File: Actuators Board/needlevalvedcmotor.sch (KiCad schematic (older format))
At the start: 46 parts, among them J10 Conn_01x02_Male, J9 Conn_01x02_Male, Q1 MMDT2222A

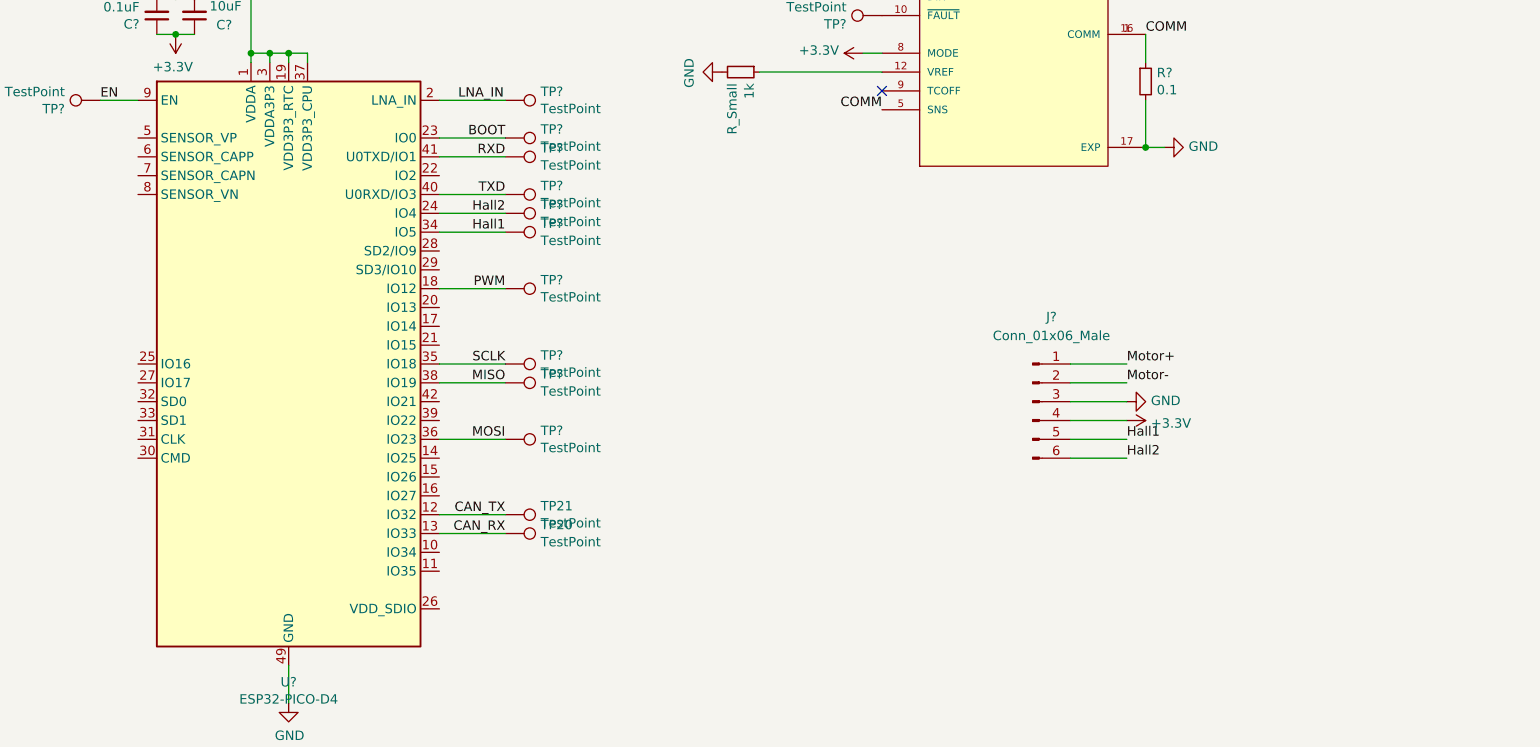
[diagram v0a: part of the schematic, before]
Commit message: Added power connectors for needlevalve
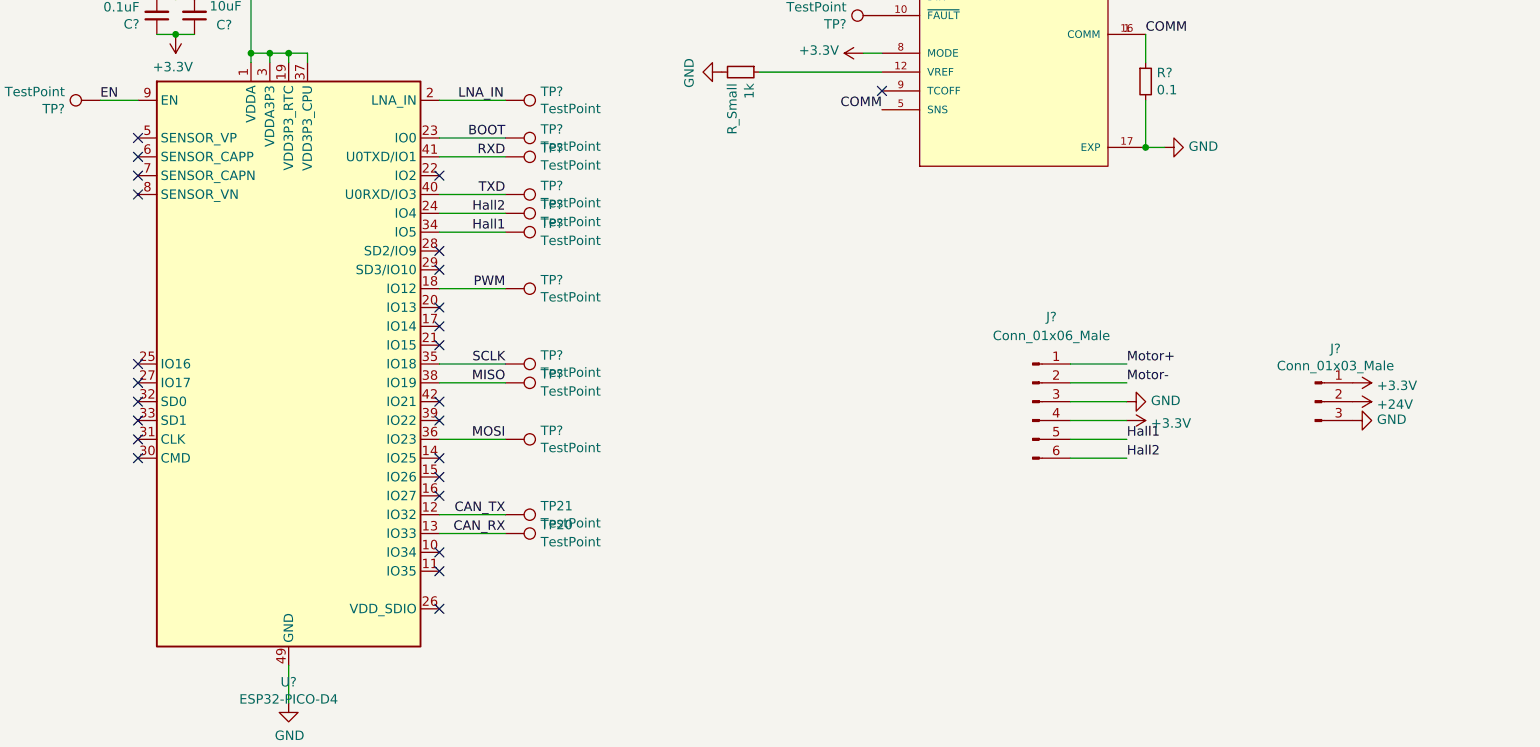
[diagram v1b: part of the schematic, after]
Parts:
- added J?: Conn_01x03_Male, symbol Connector:Conn_01x03_Male
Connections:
- net +24V: now also J?.2 (Pin_2)
- net +3V3: now also J?.1 (Pin_1)
- net GND: now also J?.3 (Pin_3)
- no-connect marks 1 -> 25
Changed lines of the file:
@@
 Wire Wire Line
 	5000 2150 5350 2150
+NoConn ~ 5000 3250
+NoConn ~ 5000 3350
+NoConn ~ 5000 3450
+NoConn ~ 5000 3750
+NoConn ~ 5000 3850
+NoConn ~ 5000 4050
+NoConn ~ 5000 4150
+NoConn ~ 5000 4250
+NoConn ~ 5000 4550
+NoConn ~ 5000 4650
+NoConn ~ 5000 4850
+NoConn ~ 5000 2550
+NoConn ~ 5000 2950
+NoConn ~ 5000 3050
+NoConn ~ 3400 3550
+NoConn ~ 3400 3650
+NoConn ~ 3400 3750
+NoConn ~ 3400 3850
+NoConn ~ 3400 3950
+NoConn ~ 3400 4050
+NoConn ~ 3400 2650
+NoConn ~ 3400 2550
+NoConn ~ 3400 2450
+NoConn ~ 3400 2350
+$Comp
+L Connector:Conn_01x03_Male J?
+U 1 1 61B4C445
+P 9650 3750
+F 0 "J?" H 9758 4031 50  0000 C CNN
+F 1 "Conn_01x03_Male" H 9758 3940 50  0000 C CNN
+F 2 "" H 9650 3750 50  0001 C CNN
+F 3 "~" H 9650 3750 50  0001 C CNN
+	1    9650 3750
+	1    0    0    -1
+$EndComp
+$Comp
+L power:+3.3V #PWR?
+U 1 1 61B4D2E9
+P 9850 3650
+F 0 "#PWR?" H 9850 3500 50  0001 C CNN
+F 1 "+3.3V" V 9865 3778 50  0000 L CNN
+F 2 "" H 9850 3650 50  0001 C CNN
+F 3 "" H 9850 3650 50  0001 C CNN
+	1    9850 3650
+	0    1    1    0
+$EndComp
+$Comp
+L power:GND #PWR?
+U 1 1 61B4E2F5
+P 9850 3850
+F 0 "#PWR?" H 9850 3600 50  0001 C CNN
+F 1 "GND" V 9855 3722 50  0000 R CNN
+F 2 "" H 9850 3850 50  0001 C CNN
+F 3 "" H 9850 3850 50  0001 C CNN
+	1    9850 3850
+	0    -1   -1   0
+$EndComp
+$Comp
+L power:+24V #PWR?
+U 1 1 61B4EDFF
+P 9850 3750
+F 0 "#PWR?" H 9850 3600 50  0001 C CNN
+F 1 "+24V" V 9865 3878 50  0000 L CNN
+F 2 "" H 9850 3750 50  0001 C CNN
+F 3 "" H 9850 3750 50  0001 C CNN
+	1    9850 3750
+	0    1    1    0
+$EndComp
 $EndSCHEMATC

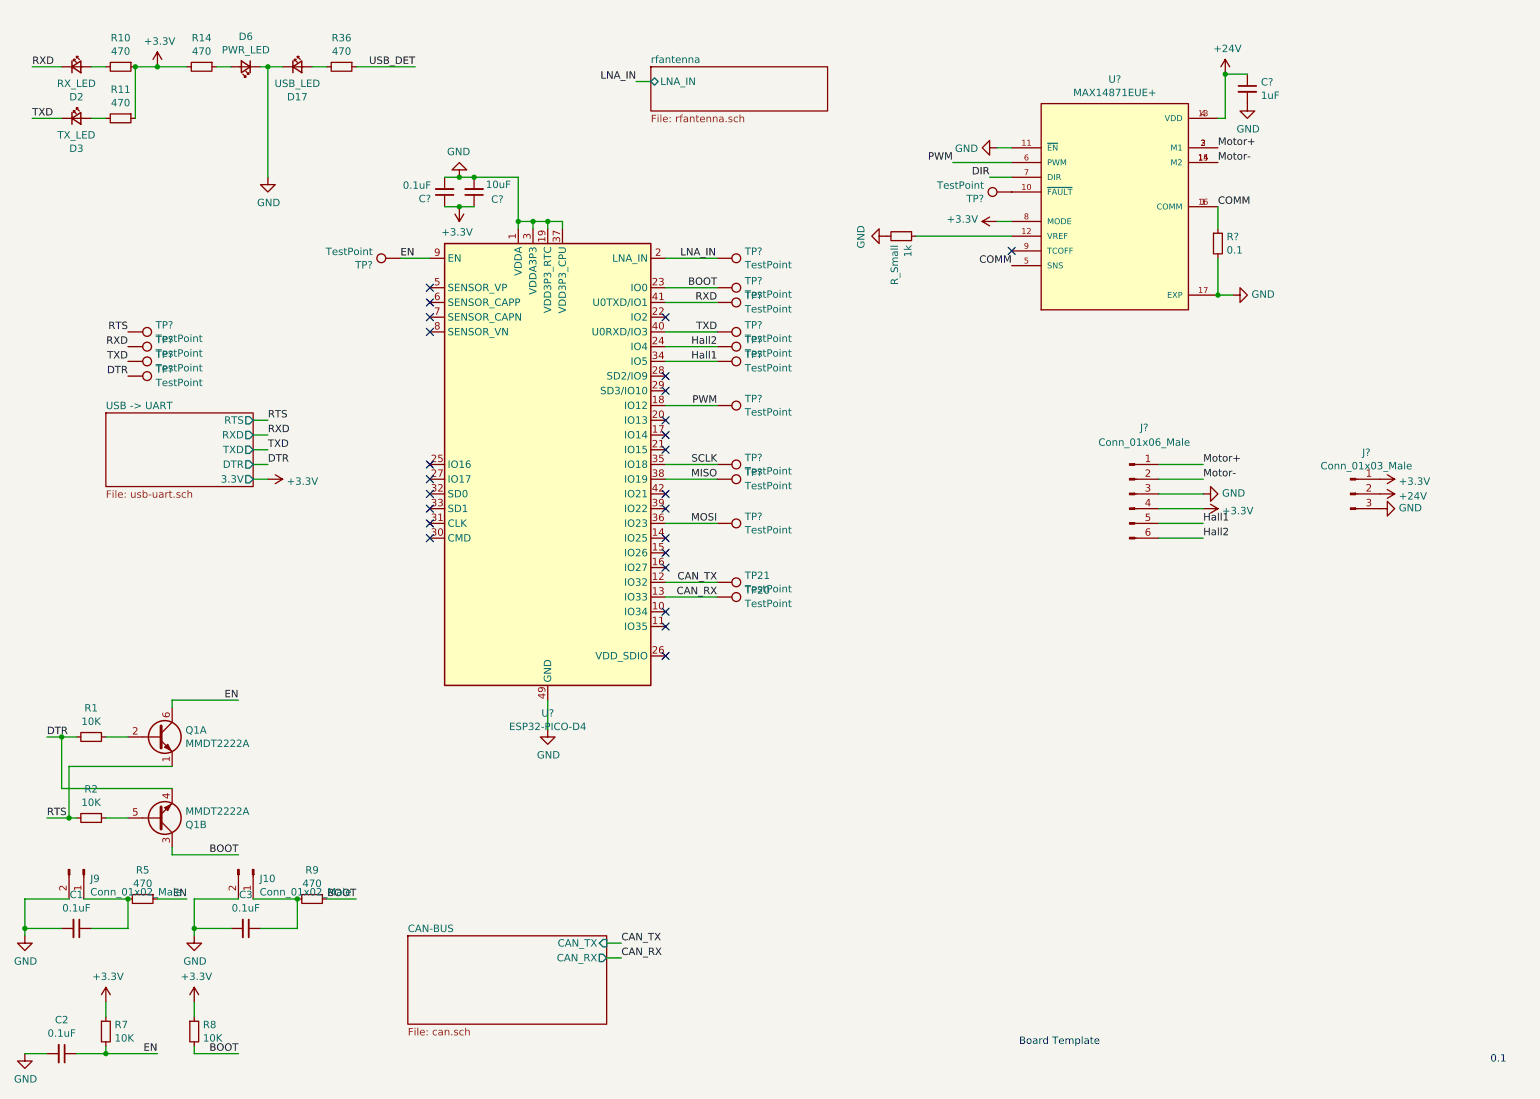
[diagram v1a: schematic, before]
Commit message: Changed main connector to 5 pins, added cool LEDs (needlevalveboard)
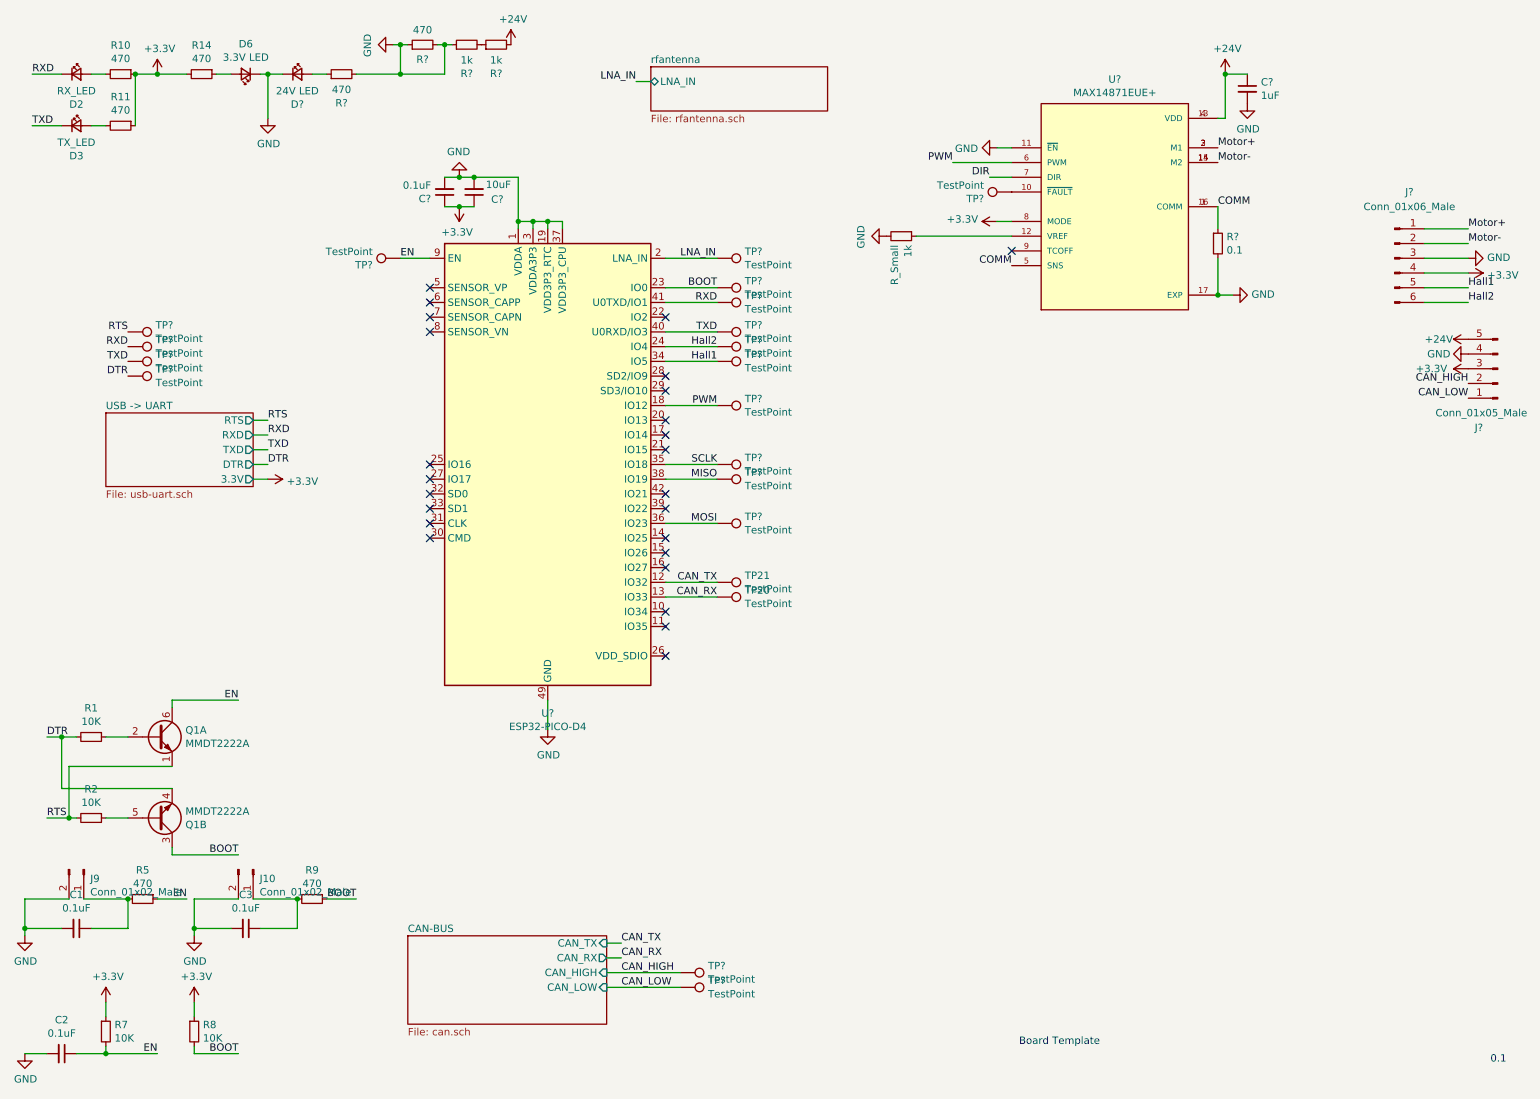
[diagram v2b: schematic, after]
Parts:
- removed D17: USB_LED, LED_SMD:LED_0603_1608Metric_Castellated, symbol Device:LED_Small
- removed J?: Conn_01x03_Male, symbol Connector:Conn_01x03_Male
- removed R36: 470, Resistor_SMD:R_0603_1608Metric, symbol Device:R_Small
- added D?: 24V LED, LED_SMD:LED_0603_1608Metric_Castellated, symbol Device:LED_Small
- added J?: Conn_01x05_Male, symbol Connector:Conn_01x05_Male
- added R? (x2): 470, Resistor_SMD:R_0603_1608Metric, symbol Device:R_Small
- added R? (x2): 1k, Resistor_SMD:R_0603_1608Metric, symbol Device:R_Small
- added TP? (x2): TestPoint, TestPoint:TestPoint_THTPad_1.0x1.0mm_Drill0.5mm, symbol Connector:TestPoint
- D6: value PWR_LED -> 3.3V LED
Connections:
- net +24V: now also J?.5 (Pin_5), R?.2
- net +3V3: now also J?.3 (Pin_3)
- net GND: now also D?.1 (K), J?.4 (Pin_4), R?.1, R?.1, R?.2, R?.2
- new net: D?.2 (A), R?.1
- new net: R?.1, R?.2
- new net CAN_HIGH: J?.2 (Pin_2), TP?.1
- new net CAN_LOW: J?.1 (Pin_1), TP?.1
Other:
- moved on the sheet: D2, D3, D6, J?, R10, R11, R14

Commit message: Connected H-Bridge Fault pin
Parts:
- removed TP? (x3): TestPoint, symbol Connector:TestPoint
- added TP?: TestPoint, symbol Connector:TestPoint
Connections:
- net SCLK is gone; now on net FAULT: U?.35 (IO18)
- net FAULT: now reaches TP?.1, U?.10 (~FAULT)
- net FAULT: now also TP?.1
- net MISO: no longer names the net of U?.38 (IO19)
- net MOSI: no longer names the net of U?.36 (IO23)
- no-connect marks 25 -> 27
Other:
- moved on the sheet: TP?
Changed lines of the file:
@@
 Text Notes 10600 7700 0    50   ~ 0
 0.1\n\n
-Text Label 5350 3650 2    50   ~ 0
-MISO
-Text Label 5350 3550 2    50   ~ 0
-SCLK
 Text Label 1550 7550 2    50   ~ 0
 EN
@@
 Wire Wire Line
 	5000 2650 5350 2650
-Wire Wire Line
-	5000 3550 5350 3550
-Wire Wire Line
-	5000 3650 5350 3650
-Wire Wire Line
-	5000 3950 5350 3950
 Text Label 5350 2450 2    50   ~ 0
 RXD
@@
 Text Label 5350 4350 2    50   ~ 0
 CAN_TX
-Text Label 5350 3950 2    50   ~ 0
-MOSI
 Wire Wire Line
 	1400 900  1550 900
@@
 $Comp
 L Connector:TestPoint TP?
-U 1 1 61B2FF39
-P 5350 3550
-F 0 "TP?" V 5304 3738 50  0000 L CNN
-F 1 "TestPoint" V 5395 3738 50  0000 L CNN
-F 2 "" H 5550 3550 50  0001 C CNN
-F 3 "~" H 5550 3550 50  0001 C CNN
-	1    5350 3550
-	0    1    1    0
-$EndComp
-$Comp
-L Connector:TestPoint TP?
-U 1 1 61B33316
-P 5350 3950
-F 0 "TP?" V 5304 4138 50  0000 L CNN
-F 1 "TestPoint" V 5395 4138 50  0000 L CNN
-F 2 "" H 5550 3950 50  0001 C CNN
-F 3 "~" H 5550 3950 50  0001 C CNN
-	1    5350 3950
-	0    1    1    0
-$EndComp
-$Comp
-L Connector:TestPoint TP?
-U 1 1 61B3A0CE
-P 5350 3650
-F 0 "TP?" V 5304 3838 50  0000 L CNN
-F 1 "TestPoint" V 5395 3838 50  0000 L CNN
-F 2 "" H 5550 3650 50  0001 C CNN
-F 3 "~" H 5550 3650 50  0001 C CNN
-	1    5350 3650
-	0    1    1    0
-$EndComp
-$Comp
-L Connector:TestPoint TP?
 U 1 1 61B41CB9
-P 7350 1700
-F 0 "TP?" V 7304 1888 50  0000 L CNN
-F 1 "TestPoint" V 7395 1888 50  0000 L CNN
-F 2 "" H 7550 1700 50  0001 C CNN
-F 3 "~" H 7550 1700 50  0001 C CNN
-	1    7350 1700
+P 7100 1700
+F 0 "TP?" V 7054 1888 50  0000 L CNN
+F 1 "TestPoint" V 7145 1888 50  0000 L CNN
+F 2 "" H 7300 1700 50  0001 C CNN
+F 3 "~" H 7300 1700 50  0001 C CNN
+	1    7100 1700
 	0    -1   -1   0
 $EndComp
@@
 Wire Wire Line
 	5000 2150 5350 2150
-NoConn ~ 5000 3250
-NoConn ~ 5000 3350
 NoConn ~ 5000 3450
 NoConn ~ 5000 3750
@@
 	0    -1   -1   0
 $EndComp
+Text Label 7350 1700 2    50   ~ 0
+FAULT
+Wire Wire Line
+	7350 1700 7100 1700
+NoConn ~ 5000 3950
+NoConn ~ 5000 3650
+NoConn ~ 5000 3250
+Text Label 5350 3550 2    50   ~ 0
+FAULT
+$Comp
+L Connector:TestPoint TP?
+U 1 1 61B8C6BC
+P 5350 3550
+F 0 "TP?" V 5304 3738 50  0000 L CNN
+F 1 "TestPoint" V 5395 3738 50  0000 L CNN
+F 2 "" H 5550 3550 50  0001 C CNN
+F 3 "~" H 5550 3550 50  0001 C CNN
+	1    5350 3550
+	0    1    1    0
+$EndComp
+Wire Wire Line
+	5000 3550 5350 3550
+NoConn ~ 5000 3350
 $EndSCHEMATC

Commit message: Added pull-up resistor to FAULT pin
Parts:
- added R?: 10k, symbol Device:R_Small
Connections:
- net +3V3: now also R?.1
- net FAULT: now also R?.2
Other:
- moved on the sheet: TP?
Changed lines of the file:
@@
 L Connector:TestPoint TP?
 U 1 1 61B41CB9
-P 7100 1700
-F 0 "TP?" V 7054 1888 50  0000 L CNN
-F 1 "TestPoint" V 7145 1888 50  0000 L CNN
-F 2 "" H 7300 1700 50  0001 C CNN
-F 3 "~" H 7300 1700 50  0001 C CNN
-	1    7100 1700
+P 6500 1700
+F 0 "TP?" V 6454 1888 50  0000 L CNN
+F 1 "TestPoint" V 6545 1888 50  0000 L CNN
+F 2 "" H 6700 1700 50  0001 C CNN
+F 3 "~" H 6700 1700 50  0001 C CNN
+	1    6500 1700
 	0    -1   -1   0
 $EndComp
@@
 Text Label 7350 1700 2    50   ~ 0
 FAULT
-Wire Wire Line
-	7350 1700 7100 1700
 NoConn ~ 5000 3950
 NoConn ~ 5000 3650
@@
 	5000 3550 5350 3550
 NoConn ~ 5000 3350
+$Comp
+L Device:R_Small R?
+U 1 1 61B55E2B
+P 6500 1600
+F 0 "R?" H 6559 1646 50  0000 L CNN
+F 1 "10k" H 6559 1555 50  0000 L CNN
+F 2 "" H 6500 1600 50  0001 C CNN
+F 3 "~" H 6500 1600 50  0001 C CNN
+	1    6500 1600
+	1    0    0    -1
+$EndComp
+Connection ~ 6500 1700
+$Comp
+L power:+3.3V #PWR?
+U 1 1 61B5708D
+P 6500 1500
+F 0 "#PWR?" H 6500 1350 50  0001 C CNN
+F 1 "+3.3V" H 6515 1673 50  0000 C CNN
+F 2 "" H 6500 1500 50  0001 C CNN
+F 3 "" H 6500 1500 50  0001 C CNN
+	1    6500 1500
+	1    0    0    -1
+$EndComp
+Wire Wire Line
+	6500 1700 7350 1700
 $EndSCHEMATC

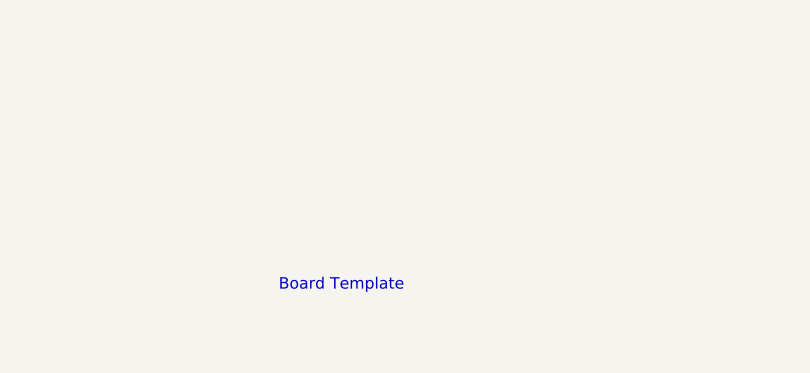
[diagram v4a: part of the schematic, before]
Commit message: Changed sheet title in title card for all boards
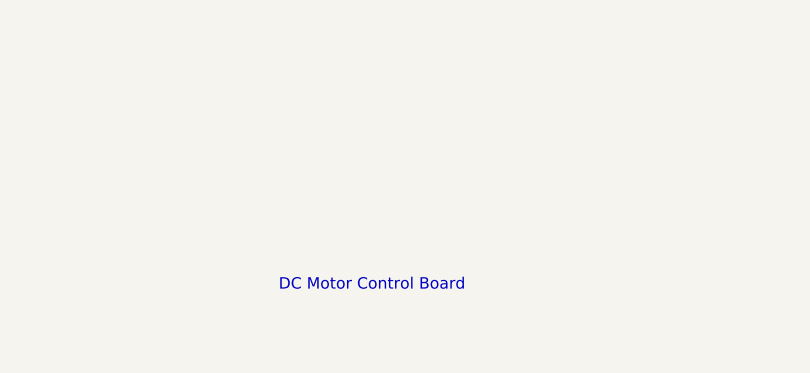
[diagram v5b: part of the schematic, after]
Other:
- note added: "DC Motor Control Board\n"
- note removed: "Board Template\n"
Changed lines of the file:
@@
 	3200 2150 3400 2150
 Text Notes 7400 7500 0    50   ~ 0
-Board Template\n
+DC Motor Control Board\n
 $Sheet
 S 1200 3200 1000 500
